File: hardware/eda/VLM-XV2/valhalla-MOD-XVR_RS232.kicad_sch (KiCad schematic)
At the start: 8 parts, among them J1 BUS, J2 RS232, J3 TTL, U1 ICL3232

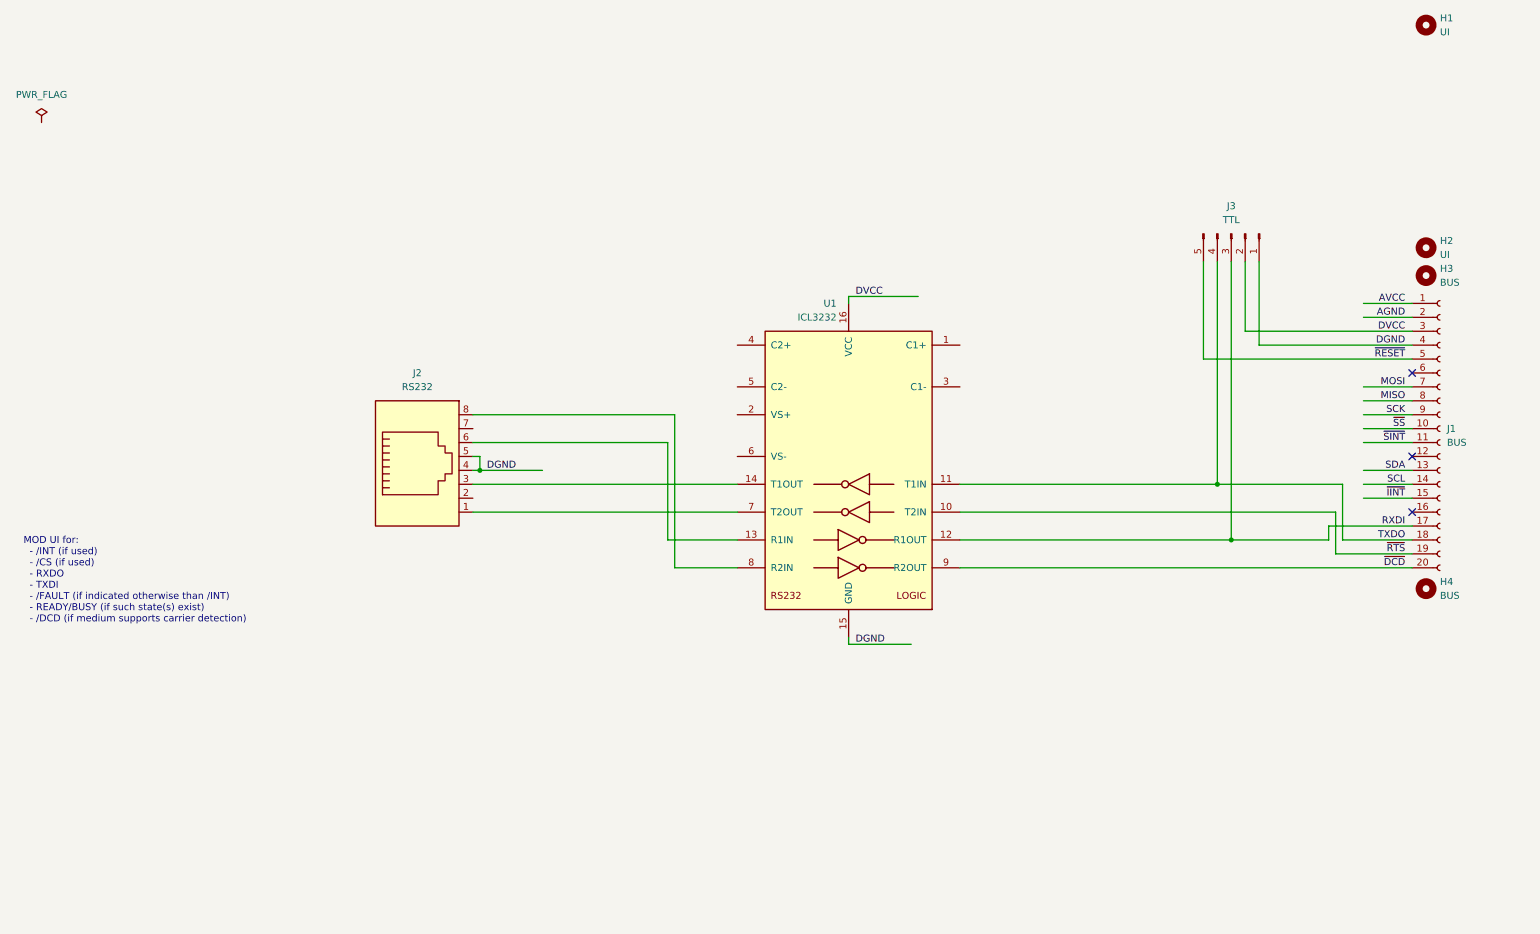
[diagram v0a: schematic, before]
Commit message: UPDATE: core transceiver part done for XVR(RS232)
  - drawn and connected core components, placed on PCB tentatively
  - will probably go for the integrated 8P8C+LEDs jack to remain
    compliant with the Valhalla-MOD mechanical standard
  - some assembly time configurability avenues identified, next to
    implement.
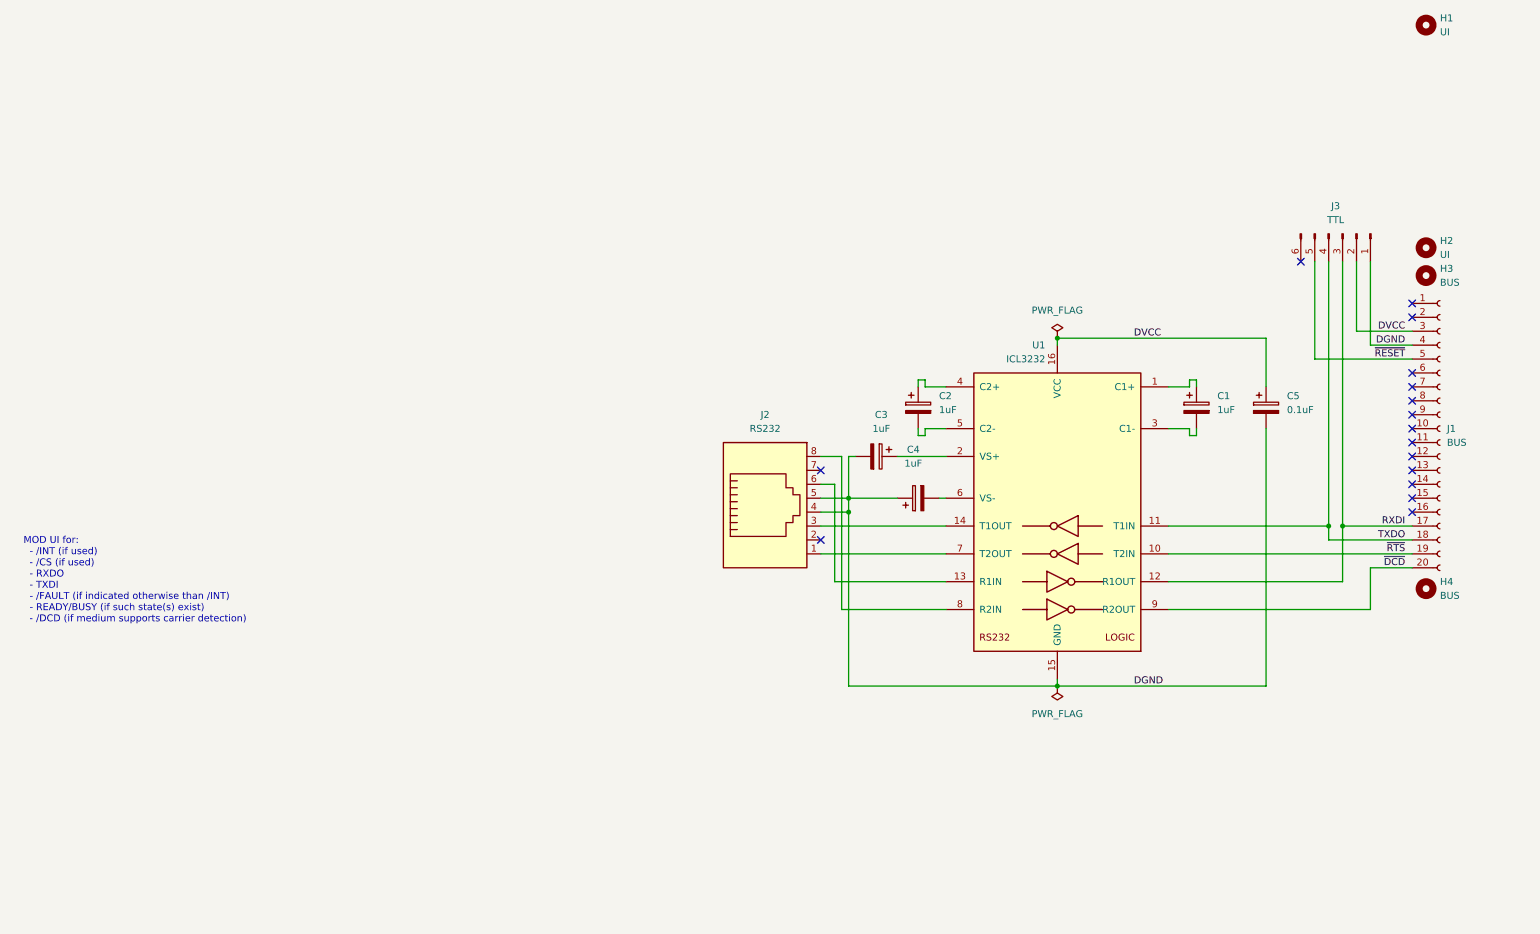
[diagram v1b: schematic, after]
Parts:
- added C1, C2, C3, C4: 1uF, Capacitor_THT:CP_Radial_D5.0mm_P2.00mm, symbol Device:C_Polarized
- added C5: 0.1uF, Capacitor_THT:C_Rect_L7.2mm_W4.5mm_P5.00mm_FKS2_FKP2_MKS2_MKP2, symbol Device:C_Polarized
- J3: footprint Connector_PinHeader_2.54mm:PinHeader_1x05_P2.54mm_Horizontal -> Connector_PinHeader_2.54mm:PinHeader_2x03_P2.54mm_Horizontal; symbol Connector:Conn_01x05_Pin -> Connector:Conn_01x06_Pin
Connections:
- net DGND: now also C3.2, C4.1, C5.2
- net DVCC: now also C5.1
- net at U1.1 (C1+): now also C1.1
- net at U1.2 (VS+): now also C3.1
- net at U1.3 (C1-): now also C1.2
- net at U1.4 (C2+): now also C2.1
- net at U1.5 (C2-): now also C2.2
- net at U1.6 (VS-): now also C4.2
- net AGND: no longer names the net of J1.2 (Pin_2)
- net AVCC: no longer names the net of J1.1 (Pin_1)
- net MISO: no longer names the net of J1.8 (Pin_8)
- net MOSI: no longer names the net of J1.7 (Pin_7)
- net SCK: no longer names the net of J1.9 (Pin_9)
- net SCL: no longer names the net of J1.14 (Pin_14)
- net SDA: no longer names the net of J1.13 (Pin_13)
- net ~{IINT}: no longer names the net of J1.15 (Pin_15)
- net ~{SINT}: no longer names the net of J1.11 (Pin_11)
- net ~{SS}: no longer names the net of J1.10 (Pin_10)
- no-connect marks 3 -> 16
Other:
- moved on the sheet: J2, U1

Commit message: UPDATE: Schematic done for XVR(RS-232)
  - gave up on native modularity in KiCAD, the data model is simply
    broken
  - routing of XVR(RS-232) to commence next.
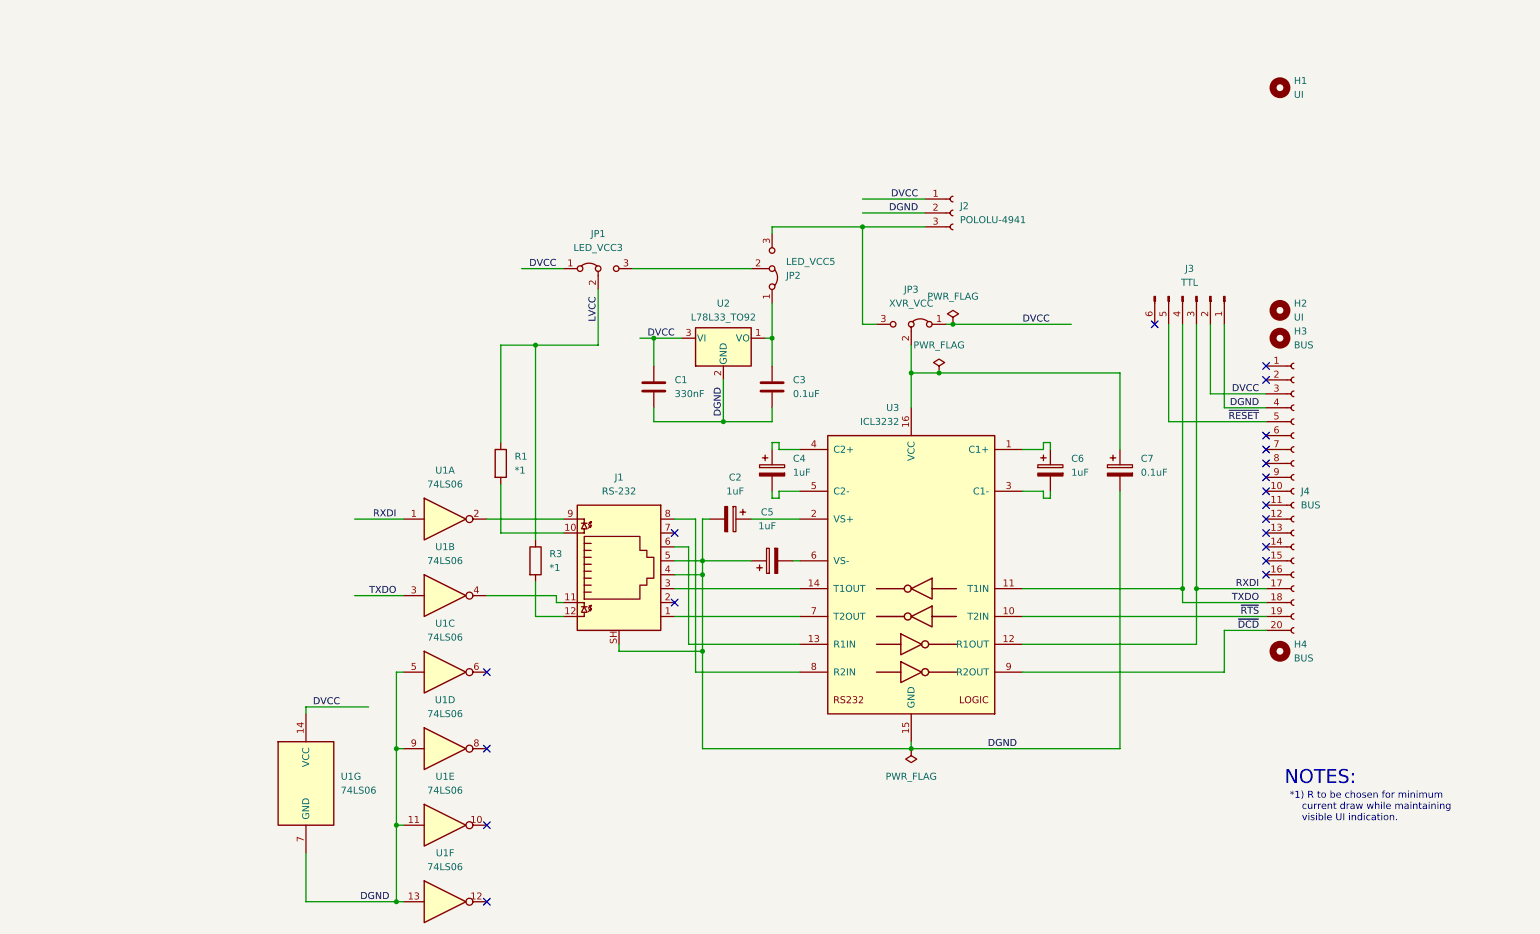
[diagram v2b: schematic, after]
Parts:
- removed J2: RS232, Connector_RJ:RJ45_Amphenol_54602-x08_Horizontal, symbol Connector:8P8C
- added C1: 330nF, Capacitor_THT:C_Rect_L4.6mm_W2.0mm_P2.50mm_MKS02_FKP02, symbol Device:C
- added C3: 0.1uF, Capacitor_THT:C_Rect_L4.6mm_W2.0mm_P2.50mm_MKS02_FKP02, symbol Device:C
- added J1: RS-232, Connector_RJ:RJ45_Amphenol_RJHSE538X, symbol Connector:8P8C_LED_Shielded
- added J2: POLOLU-4941, Connector_PinSocket_2.54mm:PinSocket_1x03_P2.54mm_Horizontal, symbol Connector:Conn_01x03_Socket
- added JP1: LED_VCC3, Connector_PinHeader_2.54mm:PinHeader_1x03_P2.54mm_Vertical, symbol Jumper:Jumper_3_Bridged12
- added JP2: LED_VCC5, Connector_PinHeader_2.54mm:PinHeader_1x03_P2.54mm_Vertical, symbol Jumper:Jumper_3_Bridged12
- added JP3: XVR_VCC, Connector_PinHeader_2.54mm:PinHeader_1x03_P2.54mm_Vertical, symbol Jumper:Jumper_3_Bridged12
- added R1, R3: *1, Resistor_THT:R_Axial_DIN0207_L6.3mm_D2.5mm_P5.08mm_Vertical, symbol Device:R
- added U1: 74LS06, symbol 74xx:74LS06
- added U2: L78L33_TO92, Package_TO_SOT_THT:TO-92_Wide, symbol Regulator_Linear:L78L33_TO92
- renumbered C3 to C2, C2 to C4, C4 to C5, C1 to C6, C5 to C7, J1 to J4, U1 to U3
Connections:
- net DGND: now also C1.2, C3.2, J1.4, J1.5, J1.SH, J2.2 (Pin_2), U1.11, U1.13, U1.5, U1.7 (GND), U1.9, U2.2 (GND)
- net DVCC: now also C1.1, J2.1 (Pin_1), JP1.1 (A), JP3.1 (A), U1.14 (VCC), U2.3 (VI); no longer C7.1, U3.16 (VCC)
- net RXDI: now also U1.1
- net TXDO: now also U1.3
- net at U3.13 (R1IN): now also J1.6
- net at U3.14 (T1OUT): now also J1.3
- net at U3.7 (T2OUT): now also J1.1
- net at U3.8 (R2IN): now also J1.8
- new net: J1.12, R3.2
- new net: J2.3 (Pin_3), JP2.3 (B), JP3.3 (B)
- new net: C7.1, JP3.2 (C), U3.16 (VCC)
- new net: JP1.3 (B), JP2.2 (C)
- new net: J1.9, U1.2
- new net: C3.1, JP2.1 (A), U2.1 (VO)
- new net: J1.10, R1.2
- new net: J1.11, U1.4
- new net LVCC: JP1.2 (C), R1.1, R3.1
- no-connect marks 16 -> 20
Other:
- note added: "*1) R to be chosen for minimum current draw while maintaining visible UI indication."
- note added: "NOTES:"
- note removed: "MOD UI for: - /INT (if used) - /CS (if used) - RXDO - TXDI - /FAULT (if indicated otherwise than /INT) - READY/BUSY (if such state(s) exist) - /DCD (if medium supports carrier detection)"
- moved on the sheet: C2, C4, C5, C6, C7, H1, H2, H3, H4, J3, J4, U3

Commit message: UPDATE: XVR(RS-232) done, RTM
  - layout and routing done for XVR(RS-232), including documentation
    for assembly variants and volumetric interference checks.
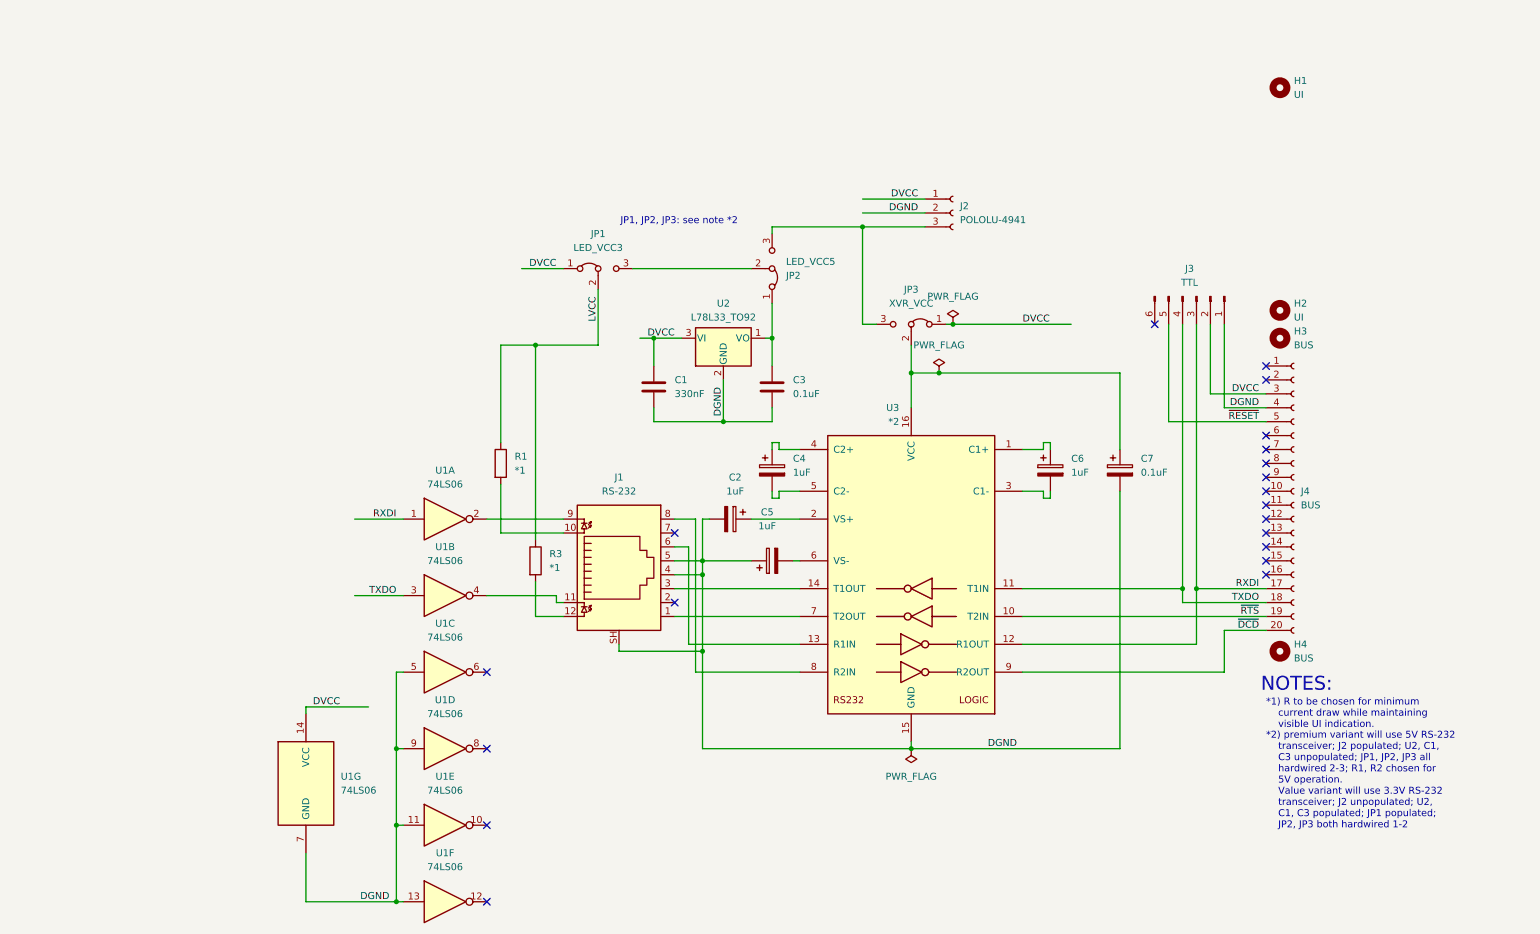
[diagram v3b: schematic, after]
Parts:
- JP2, JP3: footprint Connector_PinHeader_2.54mm:PinHeader_1x03_P2.54mm_Vertical -> Jumper:SolderJumper-3_P1.3mm_Open_RoundedPad1.0x1.5mm
- U3: value ICL3232 -> *2
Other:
- note added: "*2) premium variant will use 5V RS-232 transceiver; J2 populated; U2, C1, C3 unpopulated; JP1, JP2, JP3 all hardwired 2-3; R1, R2 chosen for 5V operation. Value variant will use 3.3V RS-232 transceiver; J2 unpopulated; U2, C1, C3 populated; JP1 populated; JP2, JP3 both hardwired 1-2"
- note added: "JP1, JP2, JP3: see note *2"
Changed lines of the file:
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@@
+		)
+	)
+	(text "JP1, JP2, JP3: see note *2"
+		(exclude_from_sim no)
+		(at 125.984 53.594 0)
+		(effects
+			(font
+				(size 1.27 1.27)
+			)
+			(justify left)
 		)
 	)
 	(text "*1) R to be chosen for minimum\n    current draw while maintaining\n    visible UI indication."
 		(exclude_from_sim no)
-		(at 248.158 160.528 0)
+		(at 243.84 143.51 0)
 		(effects
 			(font
@@
 	(text "NOTES:"
 		(exclude_from_sim no)
-		(at 253.746 155.194 0)
+		(at 249.428 138.176 0)
 		(effects
 			(font
 				(size 2.54 2.54)
 			)
+		)
+	)
+	(text "*2) premium variant will use 5V RS-232\n    transceiver; J2 populated; U2, C1,\n    C3 unpopulated; JP1, JP2, JP3 all\n    hardwired 2-3; R1, R2 chosen for\n    5V operation.\n    Value variant will use 3.3V RS-232\n    transceiver; J2 unpopulated; U2,\n    C1, C3 populated; JP1 populated;\n    JP2, JP3 both hardwired 1-2"
+		(exclude_from_sim no)
+		(at 243.84 155.702 0)
+		(effects
+			(font
+				(size 1.27 1.27)
+			)
+			(justify left)
 		)
 	)
@@
 		(length 2.54)
 		(shape round)
+		(at 153.67 78.7533 270)
+		(fields_autoplaced yes)
+		(effects
+			(font
+				(size 1.27 1.27)
+			)
+			(justify right bottom)
+		)
+		(property "Netclass" "DCD_Power"
+			(at 156.21 78.0548 90)
+			(effects
+				(font
+					(size 1.27 1.27)
+					(italic yes)
+				)
+				(justify left)
+			)
+		)
+	)
+	(netclass_flag ""
+		(length 2.54)
+		(shape round)
 		(at 181.61 149.86 180)
 		(fields_autoplaced yes)
@@
 		(property "Netclass" "DCD_Power"
 			(at 182.3085 152.4 0)
+			(effects
+				(font
+					(size 1.27 1.27)
+					(italic yes)
+				)
+				(justify left)
+			)
+		)
+	)
+	(netclass_flag ""
+		(length 2.54)
+		(shape round)
+		(at 154.94 54.61 0)
+		(fields_autoplaced yes)
+		(effects
+			(font
+				(size 1.27 1.27)
+			)
+			(justify left bottom)
+		)
+		(property "Netclass" "DCD_Power"
+			(at 155.6385 52.07 0)
 			(effects
 				(font
@@
 			)
 		)
-		(property "Value" "ICL3232"
+		(property "Value" "*2"
 			(at 176.8759 90.17 0)
 			(effects
@@
 			)
 		)
-		(property "Footprint" "Connector_PinHeader_2.54mm:PinHeader_1x03_P2.54mm_Vertical"
+		(property "Footprint" "Jumper:SolderJumper-3_P1.3mm_Open_RoundedPad1.0x1.5mm"
 			(at 179.07 72.39 0)
 			(effects
@@
 			)
 		)
-		(property "Footprint" "Connector_PinHeader_2.54mm:PinHeader_1x03_P2.54mm_Vertical"
+		(property "Footprint" "Jumper:SolderJumper-3_P1.3mm_Open_RoundedPad1.0x1.5mm"
 			(at 153.67 62.23 0)
 			(effects
